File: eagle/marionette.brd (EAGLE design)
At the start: 139.7 x 76.2 mm, 225 parts, among them J17 MA02-1, J18 MA02-1, J19 MA02-1, J2 SWD, J20 MA02-1, J22 ZX62D-B-5P8, J6 MA03-2W, J8 MA04-2W, Q1 BSS84, U1 STM32F407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

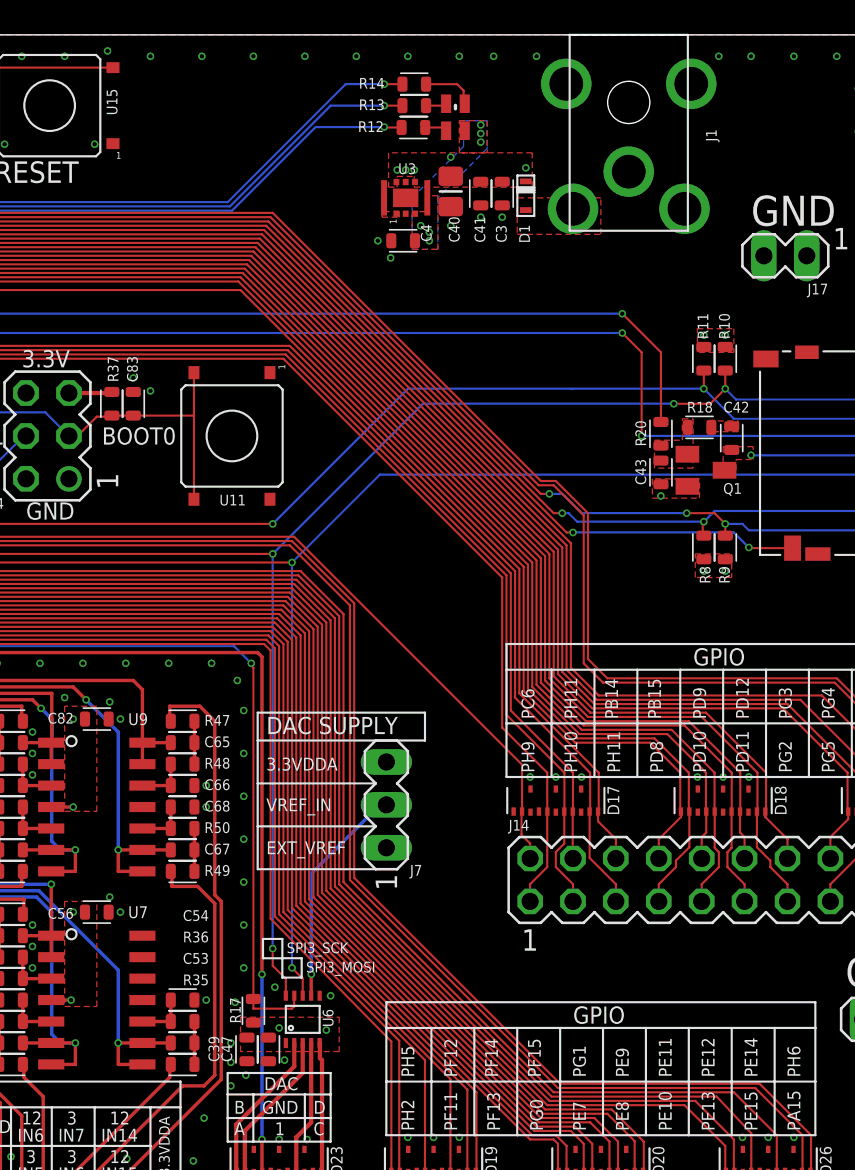
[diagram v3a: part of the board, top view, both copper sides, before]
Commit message: Replaced C42 - 0603 package with 0402 package size 0603 package size is not available
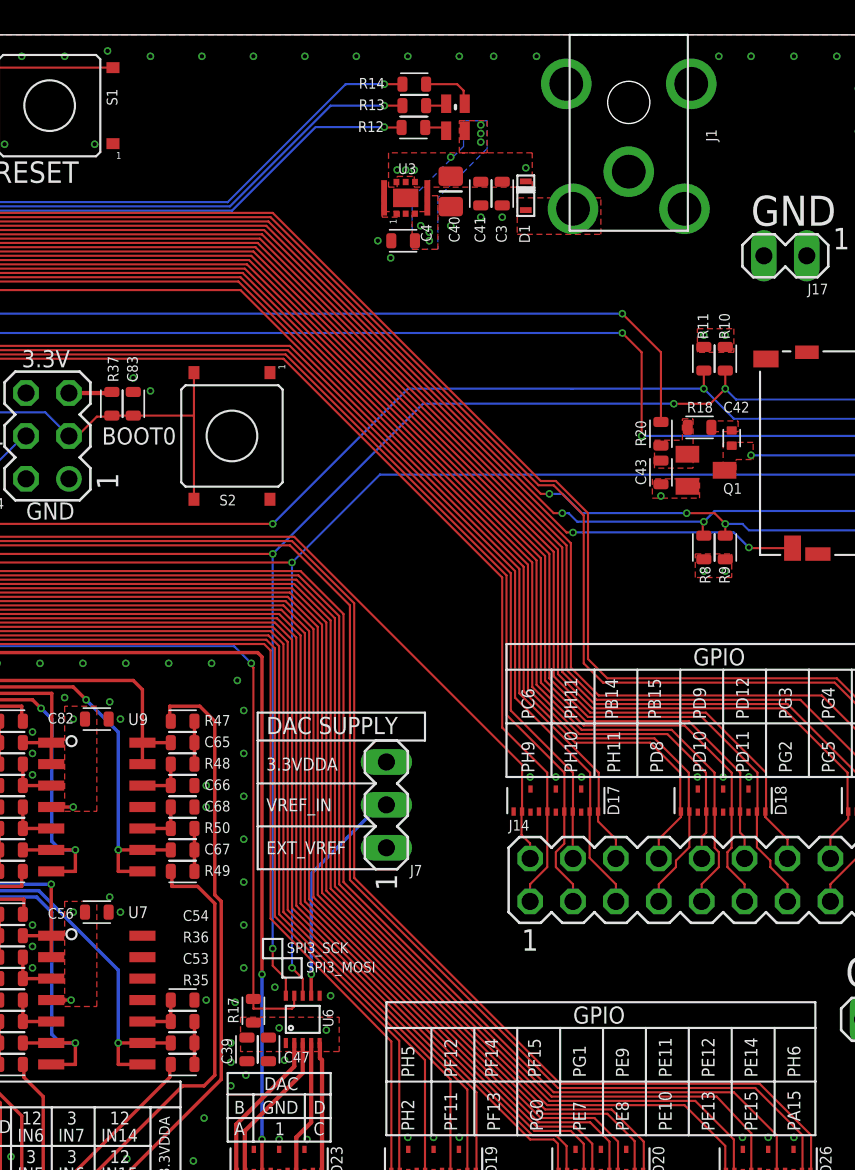
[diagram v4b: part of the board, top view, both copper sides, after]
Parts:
- C42: device rcl_custom:.0603-C -> rcl_custom:.0402-C
- C47: value 0.1uF, 10V -> 0.1uF, 10V Low ESR
- renumbered U11 to S2, U15 to S1
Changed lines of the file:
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@@
 </element>
 <element name="C39" library="rcl_custom" package=".0603-C" value="10uF, 10V" x="93.345" y="16.129" smashed="yes" rot="R270">
-<attribute name="NAME" x="91.706" y="15.383" size="0.635" layer="25" font="vector" ratio="15" rot="R90"/>
+<attribute name="NAME" x="92.468" y="15.256" size="0.635" layer="25" font="vector" ratio="15" rot="R90"/>
 <attribute name="NAME" x="93.345" y="16.129" size="0.3" layer="33" ratio="15" rot="R270" align="center"/>
 </element>
@@
 <attribute name="NAME" x="107.188" y="66.802" size="0.3" layer="33" ratio="15" rot="R270" align="center"/>
 </element>
-<element name="C42" library="rcl_custom" package=".0603-C" value="10pF" x="122.047" y="52.324" smashed="yes" rot="R90">
+<element name="C42" library="rcl_custom" package=".0402-C" value="10pF" x="122.047" y="52.324" smashed="yes" rot="R90">
 <attribute name="NAME" x="121.555" y="53.836" size="0.635" layer="25" font="vector" ratio="15"/>
 <attribute name="NAME" x="122.047" y="52.324" size="0.3" layer="33" ratio="15" rot="R90" align="center"/>
@@
 </element>
 <element name="R17" library="rcl_custom" package=".0603-C" value="4.7k" x="93.726" y="18.415" smashed="yes" rot="R270">
-<attribute name="NAME" x="92.976" y="17.669" size="0.635" layer="25" font="vector" ratio="15" rot="R90"/>
+<attribute name="NAME" x="92.849" y="17.669" size="0.635" layer="25" font="vector" ratio="15" rot="R90"/>
 <attribute name="NAME" x="93.726" y="18.415" size="0.3" layer="33" ratio="15" rot="R270" align="center"/>
 </element>
@@
 <attribute name="NAME" x="137.374" y="48.308" size="0.635" layer="25" font="vector" rot="R90"/>
 </element>
-<element name="U15" library="PTS645" package="SMT" value="PTS645" x="81.661" y="72.009" smashed="yes" rot="R180">
+<element name="S1" library="PTS645" package="SMT" value="PTS645" x="81.661" y="72.009" smashed="yes" rot="R180">
 <attribute name="NAME" x="85.038" y="73.009" size="0.635" layer="25" font="vector" ratio="20" rot="R270"/>
 </element>
@@
 <attribute name="NAME" x="18.997" y="8.648" size="0.7" layer="25" font="vector" rot="R90"/>
 </element>
-<element name="U11" library="PTS645" package="SMT" value="PTS645" x="92.456" y="52.451" smashed="yes" rot="R270">
+<element name="S2" library="PTS645" package="SMT" value="PTS645" x="92.456" y="52.451" smashed="yes" rot="R270">
 <attribute name="NAME" x="91.71" y="48.335" size="0.635" layer="25" font="vector" ratio="20"/>
 </element>
@@
 <attribute name="NAME" x="21.1718" y="52.1598" size="0.3" layer="33" ratio="15" rot="R225" align="center"/>
 </element>
-<element name="C47" library="rcl_custom" package=".0603-C" value="0.1uF, 10V" x="94.615" y="16.129" smashed="yes" rot="R270">
-<attribute name="NAME" x="92.468" y="15.383" size="0.635" layer="25" font="vector" ratio="15" rot="R90"/>
+<element name="C47" library="rcl_custom" package=".0603-C" value="0.1uF, 10V Low ESR" x="94.615" y="16.129" smashed="yes" rot="R270">
+<attribute name="NAME" x="95.52" y="15.355" size="0.635" layer="25" font="vector" ratio="15"/>
 <attribute name="VALUE" x="93.065" y="17.129" size="0.8" layer="27" font="vector" ratio="15" rot="R270"/>
 <attribute name="NAME" x="94.615" y="16.129" size="0.3" layer="33" ratio="15" rot="R270" align="center"/>
@@
 <contactref element="U1" pad="48"/>
 <contactref element="U1" pad="37"/>
-<contactref element="U15" pad="1"/>
-<contactref element="U15" pad="2"/>
+<contactref element="S1" pad="1"/>
+<contactref element="S1" pad="2"/>
 <contactref element="C31" pad="2"/>
 <contactref element="C33" pad="N"/>
@@
 <via x="29.591" y="32.766" extent="1-16" drill="0.254"/>
 <via x="33.909" y="40.894" extent="1-16" drill="0.254"/>
-<contactref element="U11" pad="2"/>
-<contactref element="U11" pad="1"/>
+<contactref element="S2" pad="2"/>
+<contactref element="S2" pad="1"/>
 <contactref element="C83" pad="2"/>
 <via x="62.23" y="4.445" extent="1-16" drill="0.254"/>
@@
 <contactref element="U1" pad="31"/>
 <contactref element="R16" pad="1"/>
-<contactref element="U15" pad="3"/>
-<contactref element="U15" pad="4"/>
+<contactref element="S1" pad="3"/>
+<contactref element="S1" pad="4"/>
 <contactref element="C31" pad="1"/>
 <wire x1="45.805590625" y1="43.859184375" x2="45.805590625" y2="43.900590625" width="0.127" layer="1"/>
@@
 <via x="123.19" y="51.308" extent="1-16" drill="0.254"/>
 <polygon width="0.127" layer="1" isolate="0.2032" thermals="no">
-<vertex x="121.539" y="51.816"/>
+<vertex x="121.539" y="52.07"/>
 <vertex x="121.539" y="50.419"/>
 <vertex x="122.301" y="50.419"/>
 <vertex x="122.301" y="51.054"/>
 <vertex x="123.317" y="51.054"/>
-<vertex x="123.317" y="51.816"/>
+<vertex x="123.317" y="52.07"/>
 </polygon>
 </signal>
@@
 <via x="59.944" y="61.214" extent="1-16" drill="0.254"/>
 <wire x1="59.944" y1="61.214" x2="61.468" y2="59.69" width="0.127" layer="16"/>
-<contactref element="U11" pad="4"/>
-<contactref element="U11" pad="3"/>
+<contactref element="S2" pad="4"/>
+<contactref element="S2" pad="3"/>
 <contactref element="C83" pad="1"/>
 <wire x1="90.206" y1="56.261" x2="90.206" y2="56.201" width="0.4064" layer="1"/>

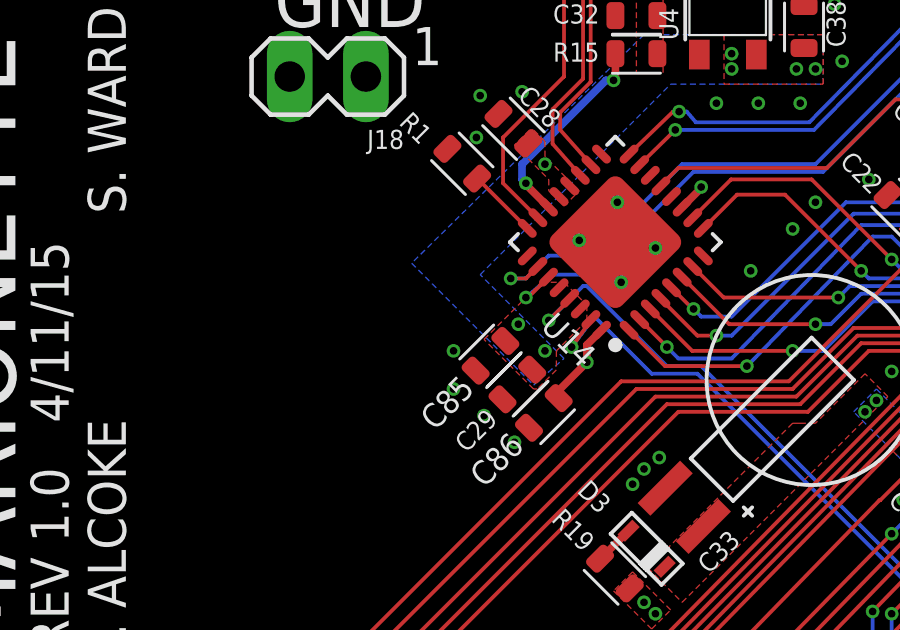
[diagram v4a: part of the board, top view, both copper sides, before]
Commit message: Connected USB_FS_VBUS to V_USB Added 0ohm resistor to ULPI did more stuff....cant remember
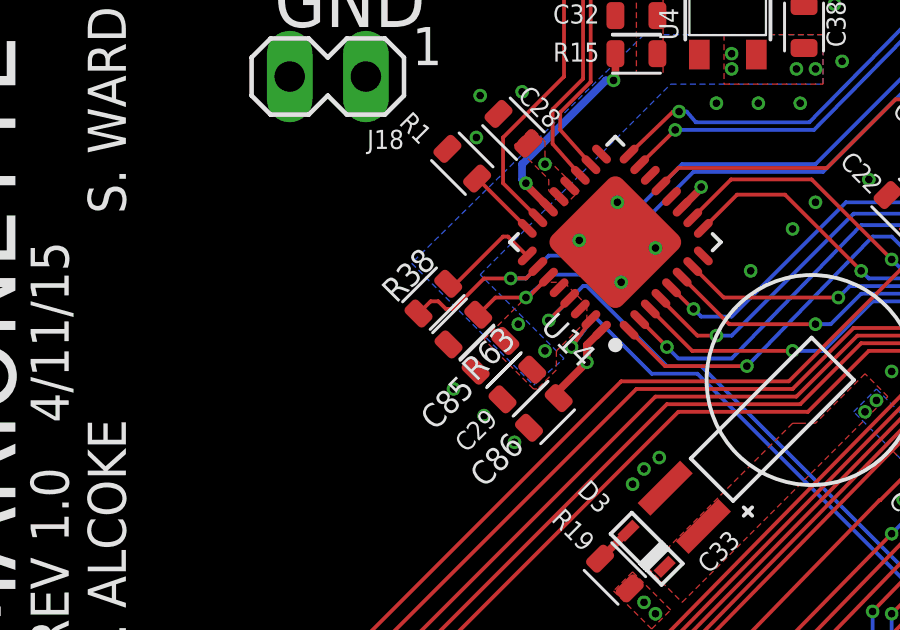
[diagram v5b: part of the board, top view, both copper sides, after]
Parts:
- added R38: 0, rcl_custom:.0603-C
- added R63: 10k, rcl_custom:.0603-C
- LED1: value (none) -> RGB
- R15: value 820 -> 10k
- U14: value (none) -> USB3320
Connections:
- removed net FS_ID: U1.121
- removed net PD5: U1.147
- removed net PI10: U1.12
- new net N$2: R38.2, U14.25
- net GND: now also R63.2
- net PB14: now also R38.1
- net PB4: now also R63.1
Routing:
- net PB14: track 57.5 -> 61.3 mm
- net N$2: track 0.00 -> 3.66 mm
- net PB4: track 23.9 -> 25.7 mm
- net GND: vias 418 -> 417
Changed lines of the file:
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@@
 <attribute name="VALUE" x="20.701" y="22.606" size="1.27" layer="27" ratio="10"/>
 </element>
-<element name="LED1" library="led-rgb-rohm" package="KINGBRITE_RGBLED_1.6X1.26" value="" x="105.6894" y="71.3232" smashed="yes" rot="R90"/>
+<element name="LED1" library="led-rgb-rohm" package="KINGBRITE_RGBLED_1.6X1.26" value="RGB" x="105.6894" y="71.3232" smashed="yes" rot="R90"/>
 <element name="Q1" library="BSS84" package="SOT23" value="BSS84" x="120.523" y="50.419" smashed="yes" rot="R270">
 <attribute name="NAME" x="121.539" y="49.022" size="0.635" layer="25"/>
@@
 <attribute name="NAME" x="103.251" y="73.279" size="0.3" layer="33" ratio="15" align="center"/>
 </element>
-<element name="R15" library="rcl_custom" package=".0603-C" value="820" x="24.257" y="64.135" smashed="yes" rot="R180">
+<element name="R15" library="rcl_custom" package=".0603-C" value="10k" x="24.257" y="64.135" smashed="yes" rot="R180">
 <attribute name="NAME" x="21.479" y="63.869" size="0.635" layer="25" font="vector" ratio="15"/>
 <attribute name="NAME" x="24.257" y="64.135" size="0.3" layer="33" ratio="15" rot="R180" align="center"/>
@@
 <attribute name="NAME" x="85.344" y="54.356" size="0.3" layer="33" ratio="15" rot="R90" align="center"/>
 </element>
-<element name="U14" library="USB3320" package="QFN32-5X5" value="" x="23.553984375" y="57.8530125" rot="R135">
+<element name="U14" library="USB3320" package="QFN32-5X5" value="USB3320" x="23.553984375" y="57.8530125" rot="R135">
 <attribute name="DMDP" value="DM" x="23.553984375" y="57.8530125" size="1.778" layer="27" rot="R135" display="off"/>
 <attribute name="DPDM" value="DP" x="23.553984375" y="57.8530125" size="1.778" layer="27" rot="R135" display="off"/>
@@
 </element>
 <element name="MCO1" library="Tova" package="10MIL-TEST-POINT" value="TEST-POINT10MIL-TEST-POINT" x="60.325" y="70.104"/>
+<element name="R38" library="rcl_custom" package=".0603-C" value="0" x="17.4888" y="55.969803125" rot="R45"/>
+<element name="R63" library="rcl_custom" package=".0603-C" value="10k" x="18.48939375" y="54.93839375" rot="R225"/>
 </elements>
 <signals>
@@
 <via x="20.447" y="62.865" extent="1-16" drill="0.254"/>
 <via x="18.923" y="61.341" extent="1-16" drill="0.254"/>
-<via x="18.161" y="54.229" extent="1-16" drill="0.254"/>
 <via x="18.161" y="52.959" extent="1-16" drill="0.254"/>
 <via x="19.177" y="52.07" extent="1-16" drill="0.254"/>
@@
 <via x="43.307" y="69.469" extent="1-16" drill="0.254"/>
 <via x="64.516" y="54.356" extent="1-16" drill="0.254"/>
+<contactref element="R63" pad="2"/>
 <wire x1="22.352" y1="57.912" x2="23.553984375" y2="57.8530125" width="0" layer="19" extent="1-1"/>
 </signal>
@@
 <wire x1="20.066" y1="56.642" x2="20.57520625" y2="56.642" width="0.127" layer="1"/>
 <wire x1="20.57520625" y1="56.642" x2="20.97304375" y2="57.0398375" width="0.127" layer="1"/>
+<contactref element="R38" pad="1"/>
+<wire x1="20.066" y1="56.642" x2="19.177" y2="56.642" width="0.127" layer="1"/>
+<wire x1="19.177" y1="56.642" x2="18.161" y2="55.626" width="0.127" layer="1"/>
+<wire x1="18.161" y1="55.626" x2="17.907" y2="55.626" width="0.127" layer="1"/>
+<wire x1="17.907" y1="55.626" x2="17.653" y2="55.88" width="0.127" layer="1"/>
+<wire x1="17.653" y1="55.88" x2="17.398996875" y2="55.88" width="0.127" layer="1"/>
+<wire x1="17.398996875" y1="55.88" x2="16.993825" y2="55.474828125" width="0.127" layer="1"/>
 </signal>
 <signal name="PC15">
@@
 <wire x1="102.551" y1="73.279" x2="101.473" y2="73.279" width="0.127" layer="1"/>
 </signal>
-<signal name="FS_ID">
-<contactref element="U1" pad="121"/>
-</signal>
 <signal name="FS_N">
 <contactref element="U1" pad="122"/>
@@
 <wire x1="39.1414" y1="63.1698" x2="33.4518" y2="63.1698" width="0.127" layer="16"/>
 <wire x1="26.162" y1="60.198" x2="30.48" y2="60.198" width="0.127" layer="16"/>
+<contactref element="R63" pad="1"/>
+<wire x1="18.984365625" y1="55.433365625" x2="19.558" y2="56.007" width="0.127" layer="1"/>
+<wire x1="19.558" y1="56.007" x2="20.574" y2="56.007" width="0.127" layer="1"/>
 </signal>
 <signal name="PB15">
@@
 <wire x1="19.431" y1="26.543" x2="19.431" y2="25.527" width="0.127" layer="1"/>
 </signal>
-<signal name="PI10">
-<contactref element="U1" pad="12"/>
-</signal>
 <signal name="PI11">
 <contactref element="U1" pad="13"/>
@@
 <wire x1="115.189" y1="28.575" x2="115.189" y2="27.432" width="0.127" layer="1"/>
 </signal>
-<signal name="PD5">
-<contactref element="U1" pad="147"/>
-</signal>
 <signal name="PD7">
 <contactref element="U1" pad="151"/>
@@
 <wire x1="41.656" y1="68.58" x2="41.656" y2="70.37" width="0.127" layer="1"/>
 </signal>
+<signal name="N$2">
+<contactref element="U14" pad="25"/>
+<contactref element="R38" pad="2"/>
+<wire x1="17.983771875" y1="56.464775" x2="18.110775" y2="56.337775" width="0.127" layer="1"/>
+<wire x1="18.110775" y1="56.337775" x2="19.812" y2="58.039" width="0.127" layer="1"/>
+<wire x1="19.812" y1="58.039" x2="19.97388125" y2="58.039" width="0.127" layer="1"/>
+<wire x1="19.97388125" y1="58.039" x2="20.619490625" y2="57.393390625" width="0.127" layer="1"/>
+</signal>
 </signals>

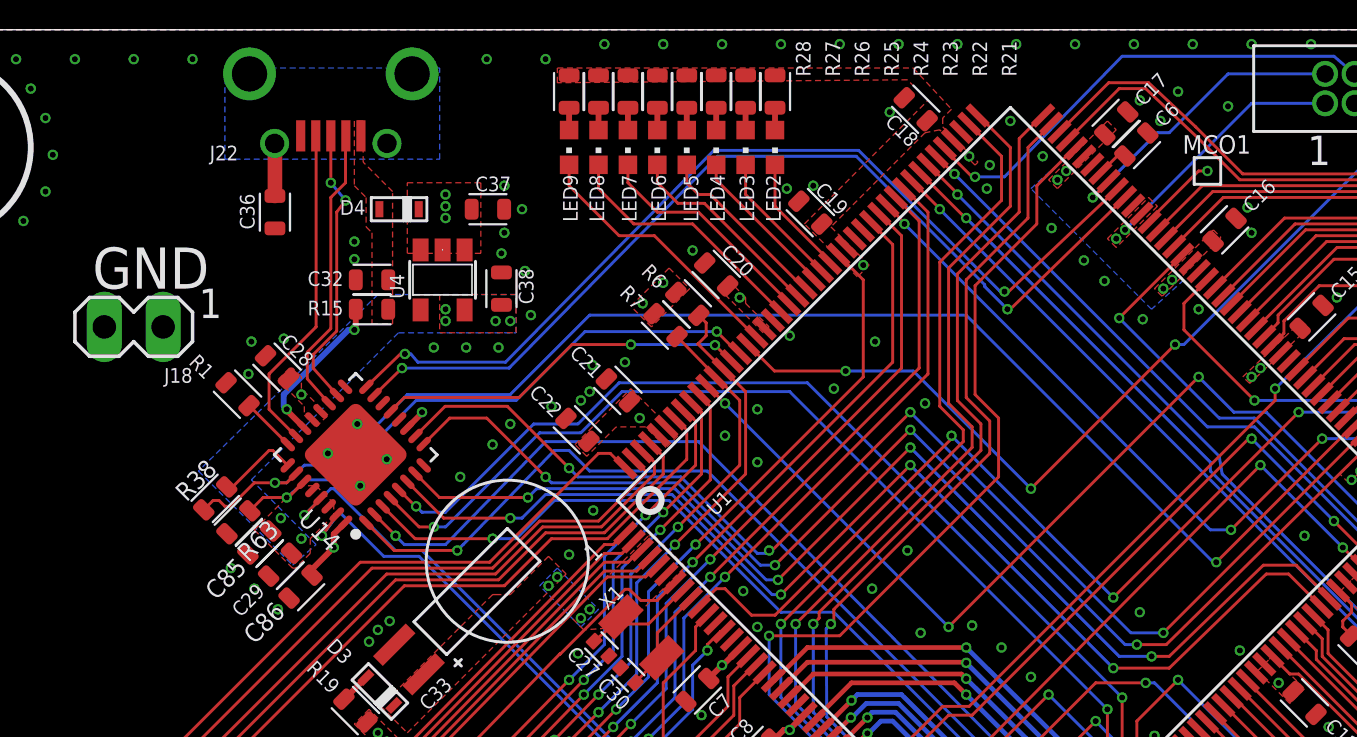
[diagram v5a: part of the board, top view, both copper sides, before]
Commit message: fixed the 0ohm resistor to ULPI
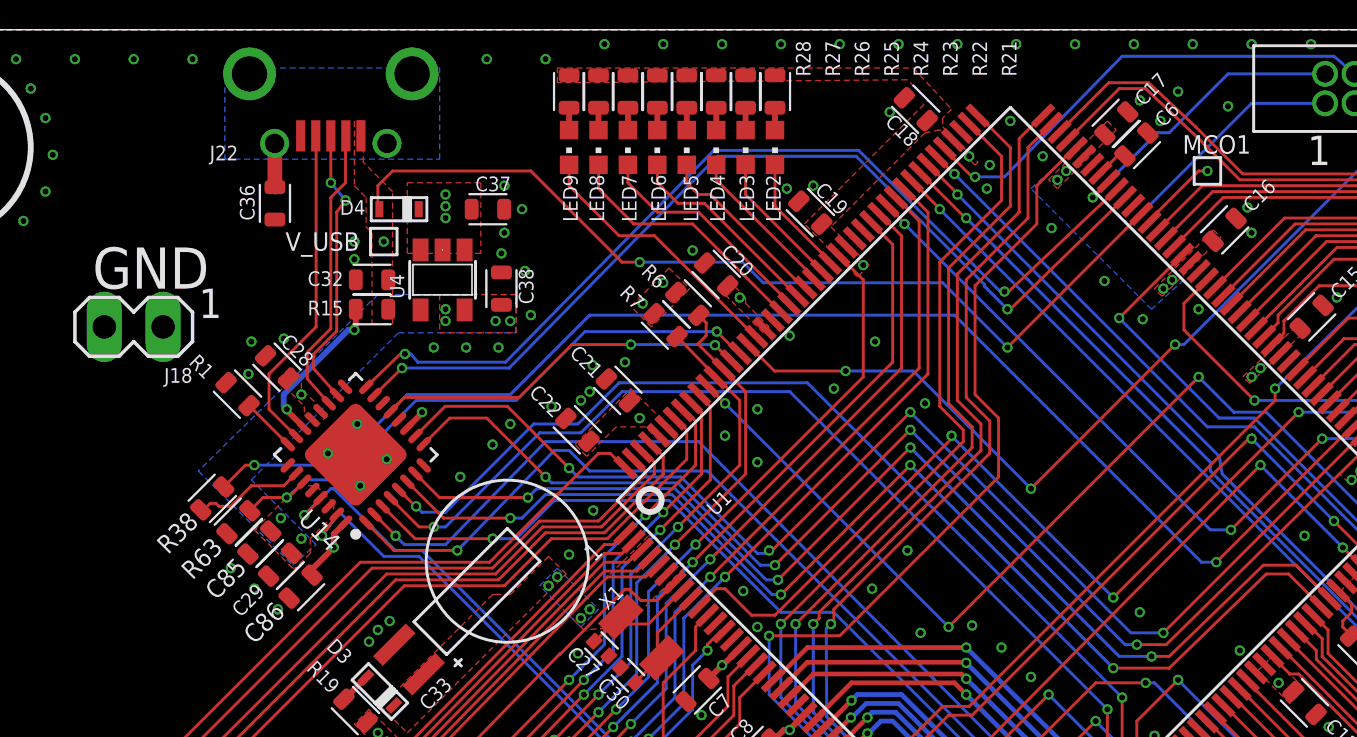
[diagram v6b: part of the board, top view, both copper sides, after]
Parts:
- added V_USB: TEST-POINT10MIL-TEST-POINT, Tova:10MIL-TEST-POINT
- moved C36 0.38 mm to (20.1, 68.7)
- moved R38 0.13 mm to (17.4, 56.0)
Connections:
- removed net N$47: C32.1, D4.P$1, J22.P1, R15.1
- new net V_USB: C32.1, D4.P$1, J22.P1, R15.1, U1.120, V_USB.P$1
- net 3.3VDD: no longer U1.120
- net N$2: now also R38.1, U14.26; no longer R38.2, U14.25
- net PB14: now also R38.2; no longer R38.1, U14.26
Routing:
- net V_USB: track 0.00 -> 39.8 mm, vias 0 -> 2
- net PB14: track 61.3 -> 58.7 mm
- net N$2: track 3.66 -> 4.86 mm
- net GND: vias 417 -> 416
- net 3.3VDD: vias 48 -> 46
- added copper zone on layer 1, net V_USB
- removed copper zone on layer 1, net N$47
